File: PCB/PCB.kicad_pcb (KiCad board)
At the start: 2 copper layers, 148.3 x 129.9 mm, 63 parts, among them J1 USB_C_Receptacle_USB2.0_16P, J2 Conn_01x15, J3 Conn_01x15, Q2 IRLML2060, SW1 TSA016A2526B, SW2 TSA016A2526B, SW3 TSA016A2526B, U1 RP2040, U2 USBLC6-2SC6, U3 NCP1117ST33T3G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

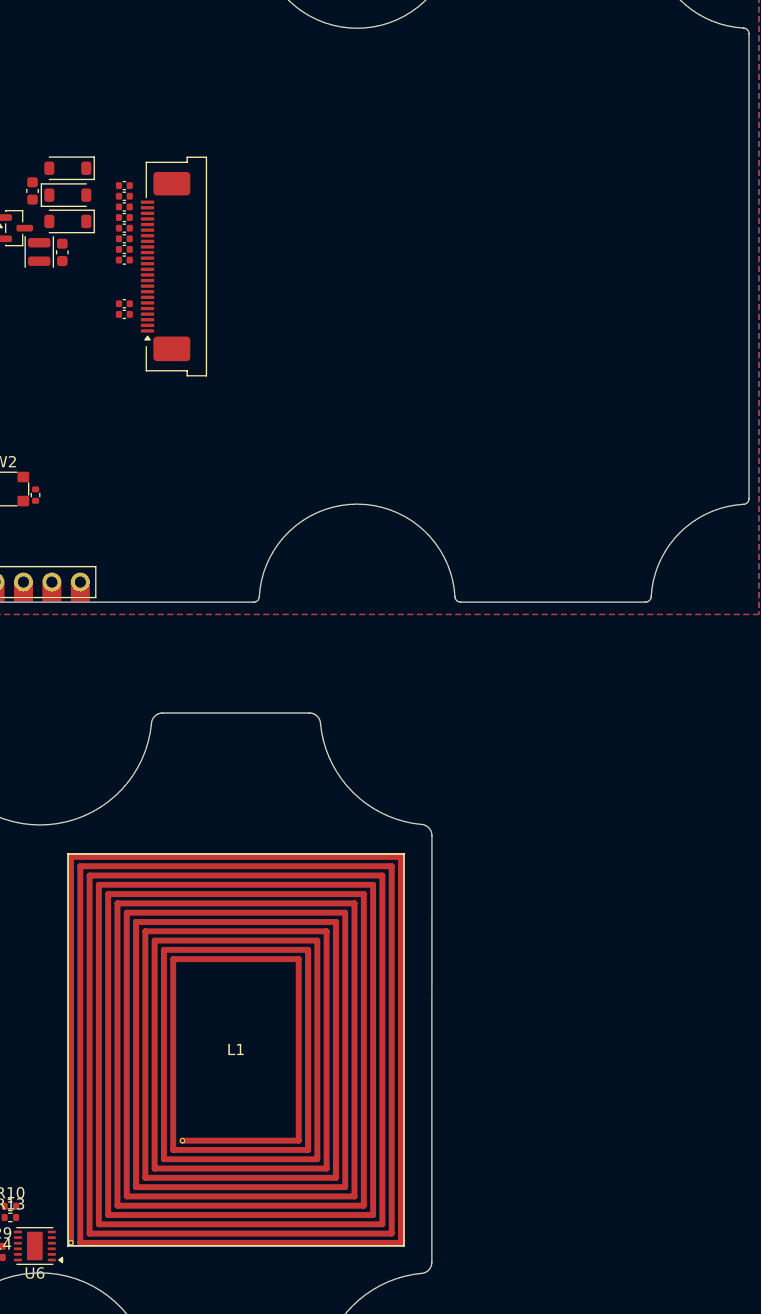
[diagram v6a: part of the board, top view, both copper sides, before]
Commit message: new NFC antenna
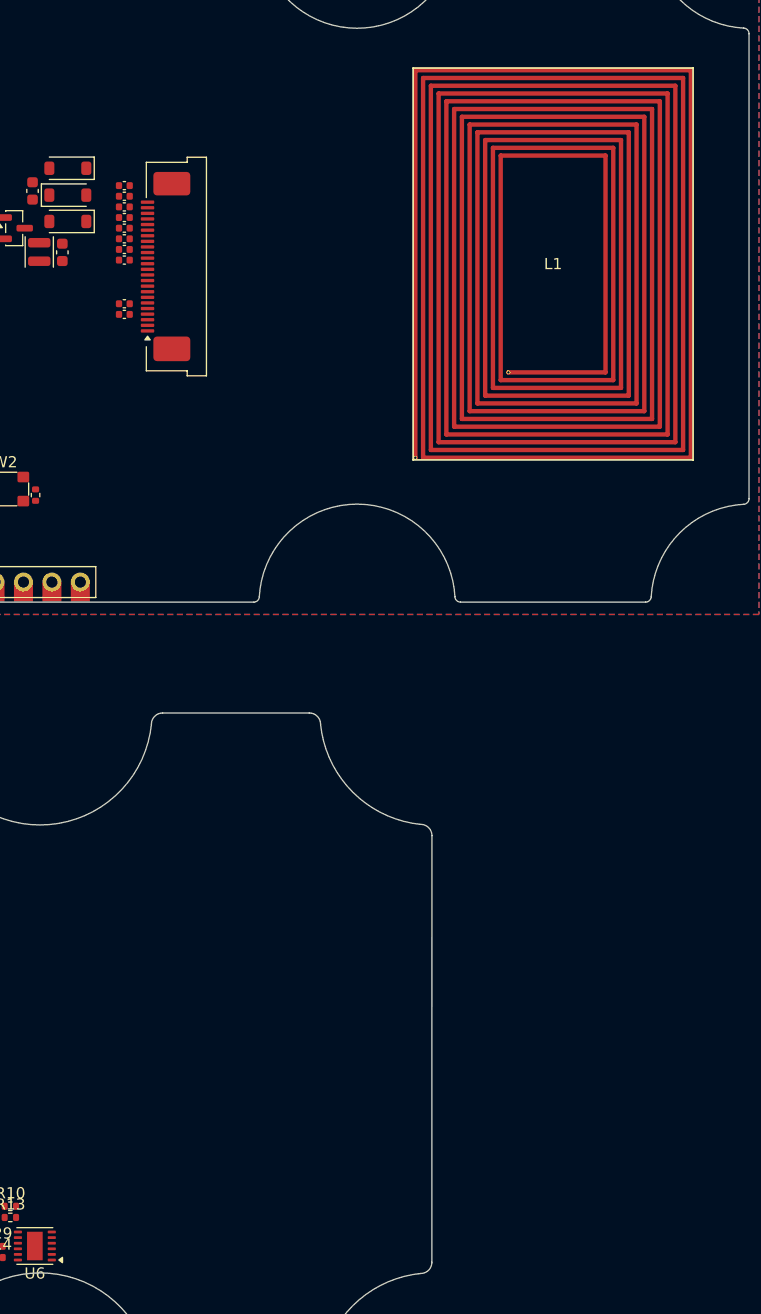
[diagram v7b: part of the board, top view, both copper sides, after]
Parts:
- L1: footprint nfc:30x35mm-antenna -> nfc:25x35mm-NFC
- moved L1 76.7 mm to (188.3, 37.4)

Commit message: finished with all the NFC stuff
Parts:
- moved R14 84.3 mm to (198.0, 73.6), turned to 180 degrees
- moved C29 82.6 mm to (198.0, 74.6), turned to 180 degrees
- moved R13 79.0 mm to (198.0, 75.6), turned to 180 degrees
- moved U6 78.8 mm to (194.9, 75.0), turned to 0 degrees
- moved R10 77.4 mm to (198.0, 76.6), turned to 180 degrees
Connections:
- L1 pad 1: Net-(U6-AC0) -> Net-(U6-AC1)
- L1 pad 2: Net-(U6-AC1) -> Net-(U6-AC0)
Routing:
- net Net-(U6-AC0): track 0.00 -> 13.1 mm, vias 0 -> 1
- net Net-(U6-AC1): track 0.00 -> 6.29 mm
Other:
- board size 148.3 x 129.9 mm -> 120 x 60 mm
